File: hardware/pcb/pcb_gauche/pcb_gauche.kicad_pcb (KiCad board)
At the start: 2 copper layers, 28 x 56 mm, 18 parts, among them P1 TE-FFC-10-0.5

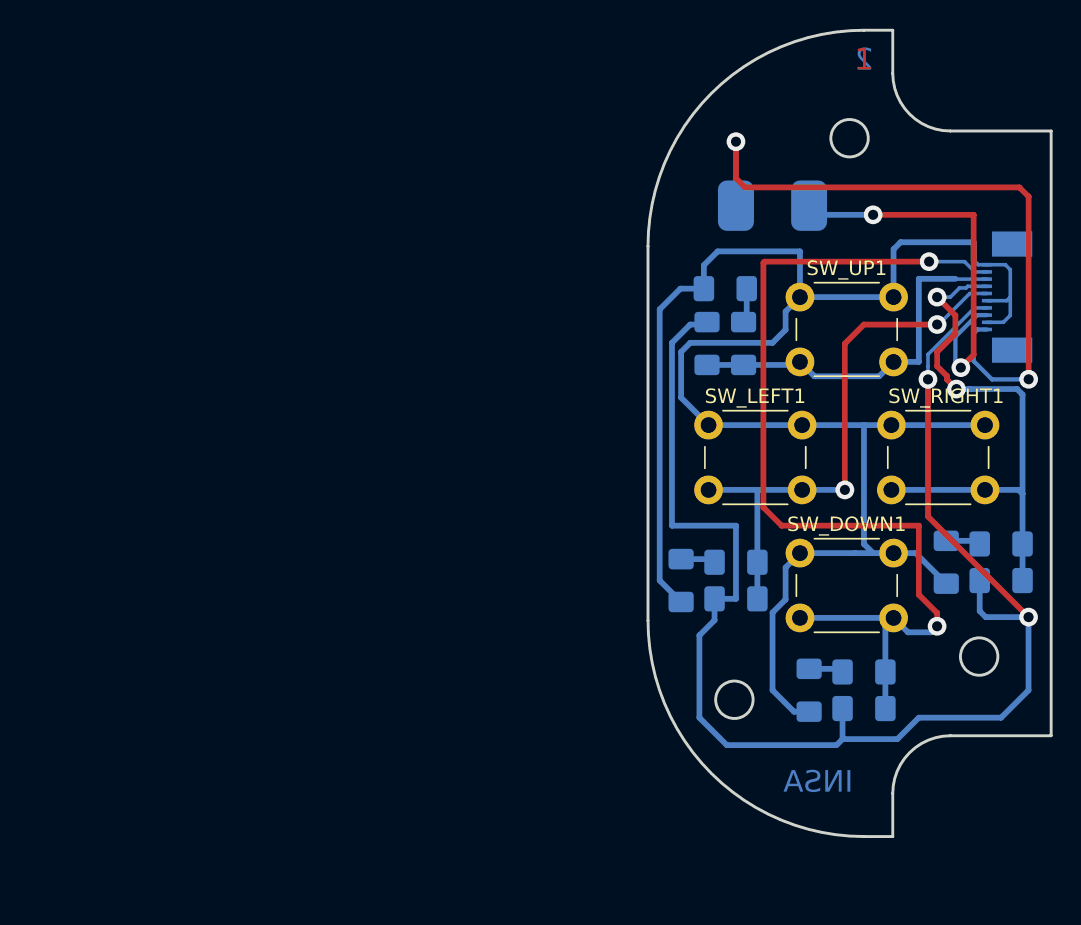
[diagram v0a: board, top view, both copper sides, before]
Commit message: Modifications des fonts et debut de la creation du drivers de touches
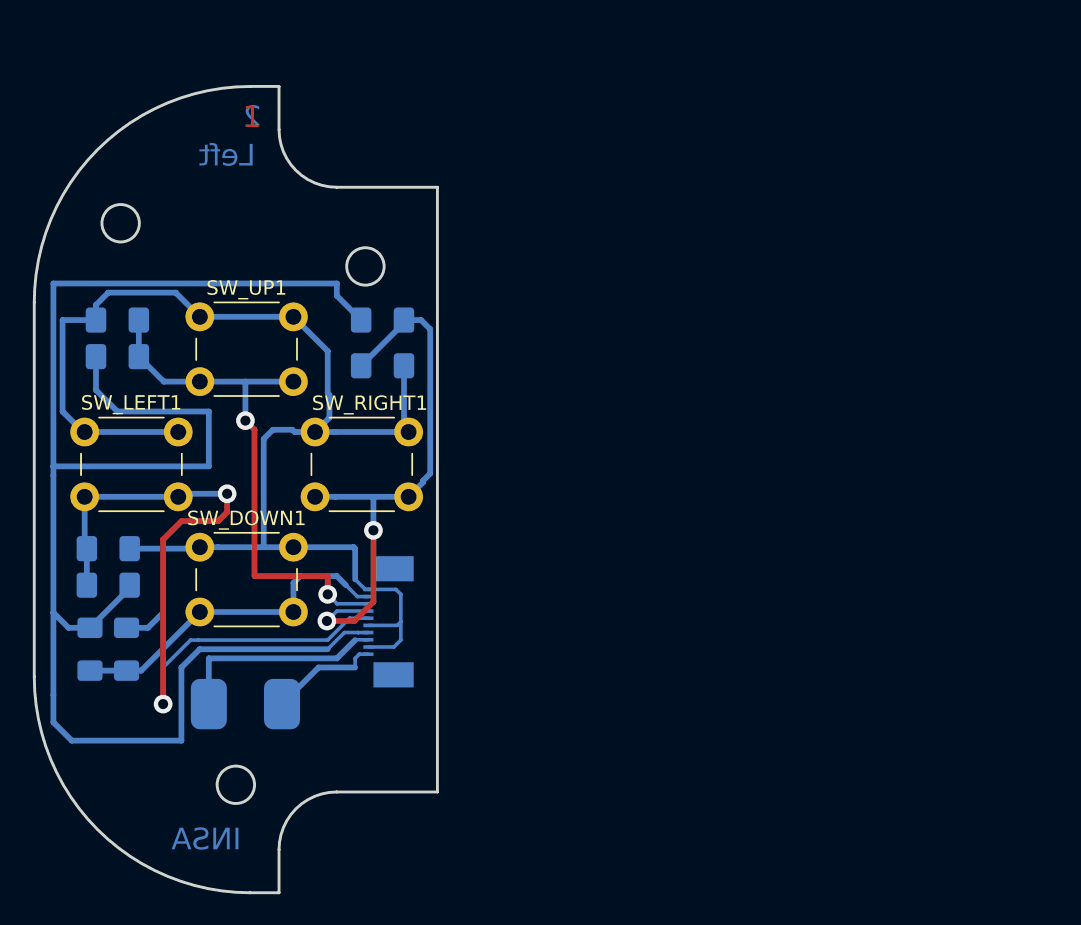
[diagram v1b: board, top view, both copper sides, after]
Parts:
- removed R2, R4, R6, R8: R, Resistor_SMD:R_1206_3216Metric_Pad1.42x1.75mm_HandSolder
- moved R3 53.9 mm to (120.9, 112.1), turned to 270 degrees
- moved LS1 50.4 mm to (131.7, 115.9), turned to 180 degrees
- moved P1 48.5 mm to (140.6, 110.2)
- moved C2 47.5 mm to (123.4, 112.1), turned to 90 degrees
- moved R7 46.6 mm to (141.2, 89.2)
- moved R5 43.6 mm to (122.1, 107.6), turned to 180 degrees
- moved SW_LEFT1 43.3 mm to (120.5, 97.0)
- moved C1 42.3 mm to (122.8, 89.2)
- moved SW_UP1 41.7 mm to (128.5, 89.0)
- moved SW_DOWN1 41.7 mm to (128.5, 105.0)
- moved C4 41.5 mm to (141.2, 92.4), turned to 0 degrees
- moved R1 41.0 mm to (122.8, 91.8), turned to 0 degrees
- moved SW_RIGHT1 40.0 mm to (136.5, 97.0)
- moved C3 39.8 mm to (122.1, 105.1), turned to 0 degrees
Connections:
- C1 pad 1: Net-(C1-Pad1) -> /Key_Up
- C2 pad 1: Net-(C2-Pad1) -> /Key_Down
- C3 pad 1: Net-(C3-Pad1) -> /Key_Left
- C4 pad 1: Net-(C4-Pad1) -> /Key_Right
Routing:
- net /Key_Down: track 68.4 -> 23.8 mm, vias 2 -> 0
- net /Audio_Left_1: track 47.8 -> 7.81 mm, vias 2 -> 0
- net GND: track 132.1 -> 102.1 mm
- net VCC: track 100.1 -> 114.4 mm, vias 2 -> 0
- net /Key_Left: track 38.3 -> 52.3 mm
- net /Audio_Left_2: track 28.1 -> 14.8 mm, vias 2 -> 0
- net /Key_Up: track 26.1 -> 37.2 mm, vias 0 -> 2
- net Net-(C1-Pad1): track 2.41 -> 0.00 mm
- net Net-(C4-Pad1): track 2.41 -> 0.00 mm
- net Net-(C3-Pad1): track 2.41 -> 0.00 mm
- net Net-(C2-Pad1): track 2.41 -> 0.00 mm
- net /Key_Right: track 38.7 -> 39.5 mm
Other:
- outline, holes or cut-outs redrawn
- board text added: "Left"

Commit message: mise a jour des pcb et design mecaniques
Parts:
- added Logo1: LOGO, Insa:insa-image, F.Cu at (129.8, 104.5)
- added REF**: MountingHole_2.7mm_M2.5, MountingHole:MountingHole_2.7mm_M2.5, F.Cu at (140.6, 86.0)
- added REF**: MountingHole_2.7mm_M2.5, MountingHole:MountingHole_2.7mm_M2.5, F.Cu at (125.6, 79.5)
- added REF**: MountingHole_2.7mm_M2.5, MountingHole:MountingHole_2.7mm_M2.5, F.Cu at (129.1, 123.5)
- C1, C2, C3, C4, LS1, P1, R1, R3, R5, R7: moved to F.Cu
- SW_DOWN1, SW_LEFT1, SW_RIGHT1, SW_UP1: footprint Button_Switch_THT:SW_PUSH_6mm -> Insa:RubberKey-4mm-2; moved to B.Cu
- moved R7 27.9 mm to (122.1, 109.5), turned to 90 degrees
- moved C4 27.6 mm to (119.6, 109.5), turned to 270 degrees
- moved SW_LEFT1 20.5 mm to (140.4, 102.1)
- moved R5 16.6 mm to (131.0, 93.7), turned to 270 degrees
- moved C3 16.2 mm to (133.6, 93.7), turned to 90 degrees
- moved SW_RIGHT1 15.4 mm to (122.0, 102.1), turned to 180 degrees
- moved P1 10.5 mm to (139.3, 99.8), turned to 270 degrees
- moved LS1 9.55 mm to (141.2, 115.3), turned to 270 degrees
- moved SW_DOWN1 6.83 mm to (131.2, 111.3), turned to 180 degrees
- moved C1 6.00 mm to (120.9, 94.9)
- moved SW_UP1 4.74 mm to (131.2, 92.9), turned to 180 degrees
- moved C2 4.49 mm to (122.8, 116.5), turned to 180 degrees
- moved R3 2.69 mm to (122.8, 114.0), turned to 0 degrees
- moved R1 2.00 mm to (120.9, 92.4)
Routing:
- net VCC: track 114.4 -> 58.2 mm
- net GND: track 102.1 -> 139.5 mm, vias 0 -> 2
- net /Key_Left: track 52.3 -> 16.9 mm, vias 2 -> 1
- net /Audio_Left_2: track 14.8 -> 32.8 mm
- net /Key_Right: track 39.5 -> 25.2 mm
- net /Audio_Left_1: track 7.81 -> 20.7 mm
- net /Key_Down: track 23.8 -> 31.9 mm, vias 0 -> 1
- net /Key_Up: track 37.2 -> 35.2 mm, vias 2 -> 1
- net (no net): track 0.00 -> 1.13 mm
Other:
- outline, holes or cut-outs redrawn
- board text added: "V.02A"
- board text removed: "INSA"
- board text removed: "Left"

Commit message: Reprise du code du firmware
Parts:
- moved SW_UP1 1.49 mm to (131.2, 91.4)
- moved SW_DOWN1 1.48 mm to (131.2, 109.8)
- moved SW_LEFT1 0.50 mm to (140.4, 101.6)
- moved SW_RIGHT1 0.50 mm to (122.0, 101.6)
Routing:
- net GND: track 139.5 -> 154.9 mm
- net /Key_Up: track 35.2 -> 36.7 mm
- net /Key_Down: track 31.9 -> 33.3 mm
- net /Key_Left: track 16.9 -> 16.3 mm
- net /Key_Right: track 25.2 -> 25.7 mm
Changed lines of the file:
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@@
     (thickness 1.6)
     (drawings 16)
-    (tracks 127)
+    (tracks 139)
     (zones 0)
     (modules 18)
@@
   )
   (module Insa:RubberKey-4mm-2 locked (layer B.Cu)
-    (at 131.2 111.275 180)
+    (at 131.2 109.8 180)
     (fp_text reference SW_DOWN1 (at 0 -3.81 180) (layer B.SilkS)
       (effects (font (size 1 1) (thickness 0.15)) (justify mirror))
@@
   )
   (module Insa:RubberKey-4mm-2 locked (layer B.Cu)
-    (at 140.385 102.1)
+    (at 140.385 101.6)
     (fp_text reference SW_LEFT1 (at -4.445 0 90) (layer B.SilkS)
       (effects (font (size 1 1) (thickness 0.15)) (justify mirror))
@@
   )
   (module Insa:RubberKey-4mm-2 locked (layer B.Cu)
-    (at 122 102.1 180)
+    (at 122 101.6 180)
     (fp_text reference SW_RIGHT1 (at 4.445 0 270) (layer B.SilkS)
       (effects (font (size 1 1) (thickness 0.15)) (justify mirror))
@@
   )
   (module Insa:RubberKey-4mm-2 locked (layer B.Cu)
-    (at 131.2 92.895 180)
+    (at 131.2 91.4 180)
     (fp_text reference SW_UP1 (at 0 4.5 180) (layer B.SilkS)
       (effects (font (size 1 1) (thickness 0.15)) (justify mirror))
@@
     (effects (font (size 1.5 1.5) (thickness 0.3)) (justify mirror))
   )
+  (segment (start 140.790001 103.594999) (end 141.19 103.195) (width 0.25) (layer F.Cu) (net 0))
+  (segment (start 140.790001 102.795001) (end 141.19 103.195) (width 0.25) (layer F.Cu) (net 0))
   (segment (start 121.2875 116.53) (end 119.6 116.53) (width 0.4) (layer F.Cu) (net 1))
   (segment (start 119.6 116.53) (end 119.6 111.0325) (width 0.4) (layer F.Cu) (net 1))
@@
   (segment (start 117.695 99.385) (end 117.695 96.5997) (width 0.4) (layer F.Cu) (net 1))
   (segment (start 117.695 110.815) (end 117.695 99.385) (width 0.4) (layer F.Cu) (net 1))
-  (segment (start 140.790001 103.594999) (end 141.19 103.195) (width 0.25) (layer F.Cu) (net 0))
-  (segment (start 140.790001 102.795001) (end 141.19 103.195) (width 0.25) (layer F.Cu) (net 0))
   (segment (start 117.695 96.5997) (end 117.695 91.13) (width 0.4) (layer F.Cu) (net 1))
   (segment (start 117.695 91.13) (end 119.6 89.225) (width 0.4) (layer F.Cu) (net 1))
-  (segment (start 128.477439 92.412561) (end 128.477439 92.472439) (width 0.4) (layer B.Cu) (net 1))
-  (segment (start 142.685 102.1) (end 143.107561 101.677439) (width 0.4) (layer B.Cu) (net 1))
-  (segment (start 143.107561 90.507561) (end 142.46 89.86) (width 0.4) (layer B.Cu) (net 1))
-  (segment (start 142.46 89.86) (end 128.49 89.86) (width 0.4) (layer B.Cu) (net 1))
-  (segment (start 128.49 89.86) (end 128.49 92.4) (width 0.4) (layer B.Cu) (net 1))
-  (segment (start 128.477439 92.472439) (end 128.9 92.895) (width 0.4) (layer B.Cu) (net 1))
-  (segment (start 128.49 92.4) (end 128.477439 92.412561) (width 0.4) (layer B.Cu) (net 1))
-  (segment (start 119.7 102.1) (end 119.7 93.57) (width 0.4) (layer B.Cu) (net 1))
-  (segment (start 128.477439 93.317561) (end 128.477439 92.472439) (width 0.4) (layer B.Cu) (net 1))
-  (segment (start 128.225 93.57) (end 128.477439 93.317561) (width 0.4) (layer B.Cu) (net 1))
-  (segment (start 119.7 93.57) (end 128.225 93.57) (width 0.4) (layer B.Cu) (net 1))
-  (segment (start 128.9 111.275) (end 120.06 111.275) (width 0.4) (layer B.Cu) (net 1))
-  (segment (start 119.7 110.915) (end 119.7 102.1) (width 0.4) (layer B.Cu) (net 1))
-  (segment (start 120.06 111.275) (end 119.7 110.915) (width 0.4) (layer B.Cu) (net 1))
   (segment (start 133.57 89.86) (end 132.935 89.225) (width 0.4) (layer F.Cu) (net 1))
   (segment (start 133.57 92.1825) (end 133.57 89.86) (width 0.4) (layer F.Cu) (net 1))
@@
   (via (at 137.38 89.86) (size 0.8) (drill 0.4) (layers F.Cu B.Cu) (net 1))
   (segment (start 138.935 99.52) (end 141.69 99.52) (width 0.25) (layer F.Cu) (net 1))
-  (via (at 141.825 99.385) (size 0.8) (drill 0.4) (layers F.Cu B.Cu) (net 1))
   (segment (start 141.69 99.52) (end 141.825 99.385) (width 0.25) (layer F.Cu) (net 1))
-  (segment (start 141.825 99.385) (end 143.107561 99.385) (width 0.4) (layer B.Cu) (net 1))
   (segment (start 143.107561 101.677439) (end 143.107561 99.385) (width 0.4) (layer B.Cu) (net 1))
-  (segment (start 143.107561 99.385) (end 143.107561 90.507561) (width 0.4) (layer B.Cu) (net 1))
   (segment (start 138.935 102.02) (end 141.095 102.02) (width 0.25) (layer F.Cu) (net 1))
   (segment (start 141.825 101.29) (end 141.825 99.385) (width 0.25) (layer F.Cu) (net 1))
   (segment (start 141.095 102.02) (end 141.825 101.29) (width 0.25) (layer F.Cu) (net 1))
+  (segment (start 142.46 89.86) (end 143.107561 90.507561) (width 0.4) (layer B.Cu) (net 1))
+  (segment (start 120.06 111.275) (end 119.7 110.915) (width 0.4) (layer B.Cu) (net 1))
+  (segment (start 119.7 110.915) (end 119.7 93.57) (width 0.4) (layer B.Cu) (net 1))
+  (segment (start 119.7 93.57) (end 128.225 93.57) (width 0.4) (layer B.Cu) (net 1))
+  (segment (start 143.107561 90.507561) (end 143.107561 99.385) (width 0.4) (layer B.Cu) (net 1))
+  (segment (start 128.477439 92.412561) (end 128.49 92.4) (width 0.4) (layer B.Cu) (net 1))
+  (segment (start 128.225 93.57) (end 128.477439 93.317561) (width 0.4) (layer B.Cu) (net 1))
+  (segment (start 128.9 111.275) (end 120.06 111.275) (width 0.4) (layer B.Cu) (net 1))
+  (segment (start 128.477439 93.317561) (end 128.477439 92.412561) (width 0.4) (layer B.Cu) (net 1))
+  (segment (start 128.9 111.275) (end 128.9 109.8) (width 0.4) (layer B.Cu) (net 1))
+  (segment (start 128.855 91.4) (end 128.49 91.765) (width 0.25) (layer B.Cu) (net 1))
+  (segment (start 128.9 91.4) (end 128.855 91.4) (width 0.25) (layer B.Cu) (net 1))
+  (segment (start 128.49 92.4) (end 128.49 91.765) (width 0.4) (layer B.Cu) (net 1))
+  (segment (start 135.475 87.955) (end 137.38 89.86) (width 0.4) (layer B.Cu) (net 1))
+  (segment (start 129.125 87.955) (end 135.475 87.955) (width 0.4) (layer B.Cu) (net 1))
+  (segment (start 128.49 91.765) (end 128.49 88.59) (width 0.4) (layer B.Cu) (net 1))
+  (segment (start 128.49 88.59) (end 129.125 87.955) (width 0.4) (layer B.Cu) (net 1))
+  (segment (start 137.38 89.86) (end 142.46 89.86) (width 0.4) (layer B.Cu) (net 1))
+  (segment (start 138.745 102.02) (end 138.205 102.56) (width 0.25) (layer F.Cu) (net 1))
+  (segment (start 138.935 102.02) (end 138.745 102.02) (width 0.25) (layer F.Cu) (net 1))
+  (segment (start 138.205 102.56) (end 138.015 102.56) (width 0.4) (layer F.Cu) (net 1))
+  (segment (start 138.015 102.56) (end 137.38 103.195) (width 0.4) (layer F.Cu) (net 1))
+  (segment (start 137.38 103.195) (end 137.38 105.735) (width 0.4) (layer F.Cu) (net 1))
+  (via (at 137.38 105.735) (size 0.8) (drill 0.4) (layers F.Cu B.Cu) (net 1))
+  (segment (start 137.38 105.735) (end 141.825 105.735) (width 0.4) (layer B.Cu) (net 1))
+  (segment (start 142.685 104.875) (end 142.685 101.6) (width 0.4) (layer B.Cu) (net 1))
+  (segment (start 141.825 105.735) (end 142.685 104.875) (width 0.4) (layer B.Cu) (net 1))
   (segment (start 141.19 117.8) (end 137.38 117.8) (width 0.4) (layer F.Cu) (net 2))
   (segment (start 137.38 117.8) (end 137.38 108.91) (width 0.4) (layer F.Cu) (net 2))
@@
   (segment (start 136.11 101.925) (end 136.11 105.735) (width 0.25) (layer F.Cu) (net 4))
   (segment (start 136.515 101.52) (end 136.11 101.925) (width 0.25) (layer F.Cu) (net 4))
+  (segment (start 133.5 111.275) (end 133.5 109.8) (width 0.4) (layer B.Cu) (net 4))
   (segment (start 122.3575 92.3722) (end 122.3575 93.67) (width 0.4) (layer F.Cu) (net 5))
   (segment (start 122.3575 93.67) (end 122.3575 94.9122) (width 0.4) (layer F.Cu) (net 5))
@@
   (segment (start 135.11 101.02) (end 134.205 101.925) (width 0.25) (layer F.Cu) (net 5))
   (segment (start 122.14 101.925) (end 134.205 101.925) (width 0.4) (layer F.Cu) (net 5))
+  (segment (start 133.5 92.895) (end 133.5 91.4) (width 0.4) (layer B.Cu) (net 5))
   (segment (start 119.6 108.0575) (end 122.14 108.0575) (width 0.4) (layer F.Cu) (net 6))
   (segment (start 122.14 108.0575) (end 123.8275 106.37) (width 0.4) (layer F.Cu) (net 6))
@@
   (segment (start 136.219694 100.52) (end 138.935 100.52) (width 0.25) (layer F.Cu) (net 6))
   (segment (start 135.869847 100.170153) (end 136.219694 100.52) (width 0.25) (layer F.Cu) (net 6))
+  (segment (start 124.3 102.1) (end 124.3 101.6) (width 0.4) (layer B.Cu) (net 6))
   (segment (start 137.662439 101.677439) (end 137.662439 99.032439) (width 0.4) (layer B.Cu) (net 7))
-  (segment (start 138.085 102.1) (end 137.662439 101.677439) (width 0.4) (layer B.Cu) (net 7))
   (segment (start 137.662439 99.032439) (end 137.38 98.75) (width 0.4) (layer B.Cu) (net 7))
   (segment (start 137.38 98.75) (end 136.11 98.75) (width 0.4) (layer B.Cu) (net 7))
